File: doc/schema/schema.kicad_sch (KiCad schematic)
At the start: 17 parts, among them M1 Motor_DC, M2 Motor_DC, U1 L293D

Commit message: fixed schematic
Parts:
- removed LM1, LM2: LM2596, symbol nucleo-l476:LM2596
- added LM1, LM2: LM2596, symbol route-runner:LM2596
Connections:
- net +3.3V: no longer QTR-HD-06A1.9 (VCC)
- net +3.3VA: now also QTR-HD-06A1.9 (VCC)
- net +5V: now also LM1.3 (VOUT)
- net +6V: now also LM2.3 (VOUT)
- net +7.4V: now also LM1.1 (VIN), LM2.1 (VIN)
- net GND: now also LM1.2 (GND), LM2.2 (GND); no longer QTR-HD-06A1.10 (GND)
- net GNDA: now also QTR-HD-06A1.10 (GND)

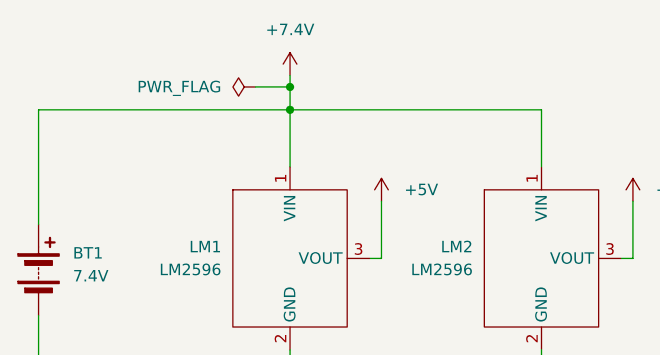
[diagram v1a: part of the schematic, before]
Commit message: Add switch to the schematic. Add readme content
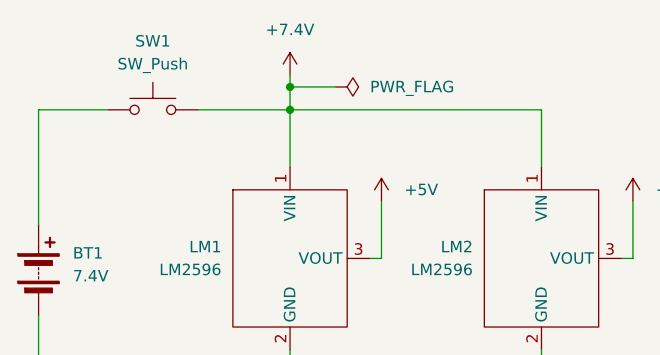
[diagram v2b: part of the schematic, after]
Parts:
- added SW1: SW_Push, symbol Switch:SW_Push
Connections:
- net +7.4V: now also SW1.2; no longer BT1.1 (+)
- new net: BT1.1 (+), SW1.1
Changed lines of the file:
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@@
-	(wire
-		(pts
-			(xy 22.86 22.86) (xy 50.8 22.86)
-		)
-		(stroke
-			(width 0)
-			(type default)
-		)
-	)
 	(wire
 		(pts
@@
 	(wire
 		(pts
+			(xy 22.86 22.86) (xy 30.48 22.86)
+		)
+		(stroke
+			(width 0)
+			(type default)
+		)
+	)
+	(wire
+		(pts
 			(xy 82.55 166.37) (xy 82.55 182.88)
 		)
@@
 	(wire
 		(pts
+			(xy 40.64 22.86) (xy 50.8 22.86)
+		)
+		(stroke
+			(width 0)
+			(type default)
+		)
+	)
+	(wire
+		(pts
 			(xy 261.62 77.47) (xy 261.62 80.01)
 		)
@@
 	(wire
 		(pts
-			(xy 46.99 20.32) (xy 50.8 20.32)
+			(xy 55.88 20.32) (xy 50.8 20.32)
 		)
 		(stroke
@@
 	)
 	(symbol
-		(lib_id "power:PWR_FLAG")
-		(at 46.99 20.32 90)
+		(lib_id "Switch:SW_Push")
+		(at 35.56 22.86 0)
 		(unit 1)
 		(exclude_from_sim no)
@@
 		(dnp no)
 		(fields_autoplaced yes)
+		(property "Reference" "SW1"
+			(at 35.56 15.24 0)
+			(effects
+				(font
+					(size 1.27 1.27)
+				)
+			)
+		)
+		(property "Value" "SW_Push"
+			(at 35.56 17.78 0)
+			(effects
+				(font
+					(size 1.27 1.27)
+				)
+			)
+		)
+		(property "Footprint" ""
+			(at 35.56 17.78 0)
+			(effects
+				(font
+					(size 1.27 1.27)
+				)
+				(hide yes)
+			)
+		)
+		(property "Datasheet" "~"
+			(at 35.56 17.78 0)
+			(effects
+				(font
+					(size 1.27 1.27)
+				)
+				(hide yes)
+			)
+		)
+		(property "Description" "Push button switch, generic, two pins"
+			(at 35.56 22.86 0)
+			(effects
+				(font
+					(size 1.27 1.27)
+				)
+				(hide yes)
+			)
+		)
+		(pin "2"
+		)
+		(pin "1"
+		)
+		(instances
+			(project ""
+				(path "/fdd85666-e408-451c-91f4-9eba5bc098ae"
+					(reference "SW1")
+					(unit 1)
+				)
+			)
+		)
+	)
+	(symbol
+		(lib_id "power:PWR_FLAG")
+		(at 55.88 20.32 270)
+		(unit 1)
+		(exclude_from_sim no)
+		(in_bom yes)
+		(on_board yes)
+		(dnp no)
+		(fields_autoplaced yes)
 		(property "Reference" "#FLG01"
-			(at 45.085 20.32 0)
+			(at 57.785 20.32 0)
 			(effects
 				(font
@@
 		)
 		(property "Value" "PWR_FLAG"
-			(at 43.18 20.3199 90)
+			(at 59.69 20.3199 90)
 			(effects
 				(font
@@
 		)
 		(property "Footprint" ""
-			(at 46.99 20.32 0)
+			(at 55.88 20.32 0)
 			(effects
 				(font
@@
 		)
 		(property "Datasheet" "~"
-			(at 46.99 20.32 0)
+			(at 55.88 20.32 0)
 			(effects
 				(font
@@
 		)
 		(property "Description" "Special symbol for telling ERC where power comes from"
-			(at 46.99 20.32 0)
-			(effects
-				(font
+			(at 55.88 20.32 0)
+			(effects
+				(font

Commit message: Documentation update
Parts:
- removed D2, D3: LED, symbol Device:LED
- removed NUCLEO-L1: NUCLEO-L476, symbol route-runner:nucleo-l476
- removed ST1: ST1089, symbol route-runner:ST1089
- added DS1: ~, symbol route-runner:ds2-socket
- added NUCLEO-F1: ~, symbol route-runner:nucleo-f303
- R2, R3: value 1k -> 100
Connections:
- net DIAG_RED is gone; now on net +3.3VA: R3.1
- net GNDA is gone; now on net GND: QTR-HD-06A1.10 (GND)
- net +3.3V: now also DS1. (VCC), NUCLEO-F1. (VIN)
- net +3.3VA: now also R2.2, NUCLEO-F1. (VIN)
- net +5V: now also NUCLEO-F1. (VIN)
- net DIAG_GRN: now also NUCLEO-F1. (VIN)
- net GND: now also DS1. (VCC), NUCLEO-F1. (VIN)
- net LNSENS_CH1: now also NUCLEO-F1. (VIN)
- net LNSENS_CH2: now also NUCLEO-F1. (VIN)
- net LNSENS_CH3: now also NUCLEO-F1. (VIN)
- net LNSENS_CH4: now also NUCLEO-F1. (VIN)
- net LNSENS_CH5: now also NUCLEO-F1. (VIN)
- net LNSENS_CH6: now also NUCLEO-F1. (VIN)
- net at M2.1 (+): now also U1.11 (3Y); no longer U1.14 (4Y)
- net at M2.2 (-): now also U1.14 (4Y); no longer U1.11 (3Y)
- net at R3.2: now also NUCLEO-F1. (VIN)
- net at U1.3 (1Y): now also M1.2 (-); no longer M1.1 (+)
- net at U1.6 (2Y): now also M1.1 (+); no longer M1.2 (-)
- net DIAG_YEL: no longer names the net of R2.1
- net DIAG_YEL: now also NUCLEO-F1. (VIN)
- net M1_CTR_1 renamed MR_CTR_1
- net MR_CTR_1: now also NUCLEO-F1. (VIN)
- net M1_CTR_2 renamed MR_CTR_2
- net MR_CTR_2: now also NUCLEO-F1. (VIN)
- net M1_PWM renamed MR_PWM
- net MR_PWM: now also NUCLEO-F1. (VIN)
- net M2_CTR_1 renamed ML_CTR_1
- net ML_CTR_1: now also NUCLEO-F1. (VIN)
- net M2_CTR_2 renamed ML_CTR_2
- net ML_CTR_2: now also NUCLEO-F1. (VIN)
- net M2_PWM renamed ML_PWM
- net ML_PWM: now also NUCLEO-F1. (VIN)
- new net DS2_CS: DS1. (VCC), NUCLEO-F1. (VIN)
- new net DS2_MISO: DS1. (VCC), NUCLEO-F1. (VIN)
- new net DS2_MOSI: DS1. (VCC), NUCLEO-F1. (VIN)
- new net DS2_SCK: DS1. (VCC), NUCLEO-F1. (VIN)
- no-connect marks 2 -> 8
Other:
- moved on the sheet: C1, C2, D1, M1, M2, R1

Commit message: documentation update
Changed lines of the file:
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@@
 		(color 0 0 0 0)
 	)
+	(junction
+		(at 50.8 60.96)
+		(diameter 0)
+		(color 0 0 0 0)
+	)
 	(no_connect
 		(at 77.47 152.4)
@@
 	(wire
 		(pts
+			(xy 50.8 60.96) (xy 50.8 62.23)
+		)
+		(stroke
+			(width 0)
+			(type default)
+		)
+	)
+	(wire
+		(pts
 			(xy 205.74 48.26) (xy 217.17 48.26)
 		)
@@
 	(wire
 		(pts
-			(xy 50.8 57.15) (xy 50.8 62.23)
+			(xy 50.8 57.15) (xy 50.8 60.96)
 		)
 		(stroke
@@
 	(wire
 		(pts
+			(xy 50.8 60.96) (xy 57.15 60.96)
+		)
+		(stroke
+			(width 0)
+			(type default)
+		)
+	)
+	(wire
+		(pts
 			(xy 242.57 29.21) (xy 242.57 33.02)
 		)
@@
 					(unit 1)
 				)
+			)
+		)
+	)
+	(symbol
+		(lib_id "power:PWR_FLAG")
+		(at 57.15 60.96 270)
+		(unit 1)
+		(exclude_from_sim no)
+		(in_bom yes)
+		(on_board yes)
+		(dnp no)
+		(fields_autoplaced yes)
+		(property "Reference" "#FLG02"
+			(at 59.055 60.96 0)
+			(effects
+				(font
+					(size 1.27 1.27)
+				)
+				(hide yes)
+			)
+		)
+		(property "Value" "PWR_FLAG"
+			(at 60.96 60.9599 90)
+			(effects
+				(font
+					(size 1.27 1.27)
+				)
+				(justify left)
+			)
+		)
+		(property "Footprint" ""
+			(at 57.15 60.96 0)
+			(effects
+				(font
+					(size 1.27 1.27)
+				)
+				(hide yes)
+			)
+		)
+		(property "Datasheet" "~"
+			(at 57.15 60.96 0)
+			(effects
+				(font
+					(size 1.27 1.27)
+				)
+				(hide yes)
+			)
+		)
+		(property "Description" "Special symbol for telling ERC where power comes from"
+			(at 57.15 60.96 0)
+			(effects
+				(font
+					(size 1.27 1.27)
+				)
+				(hide yes)
+			)
+		)
+		(pin "1"
+		)
+		(instances
+			(project "schema"
+				(path "/fdd85666-e408-451c-91f4-9eba5bc098ae"
+					(reference "#FLG02")
+					(unit 1)
+				)
